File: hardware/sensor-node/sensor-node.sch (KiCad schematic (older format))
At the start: 51 parts, among them J1 CONUFL001-SMD-T, J2 Conn_ARM_JTAG_SWD_10, Q1 PMV250EPEA, U1 TLV61225, U2 TPS27081A, U3 SHT31-DIS, U4 24LC32, U5 MLX90614, U6 ADG633YCP, U7 TSV911RILT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

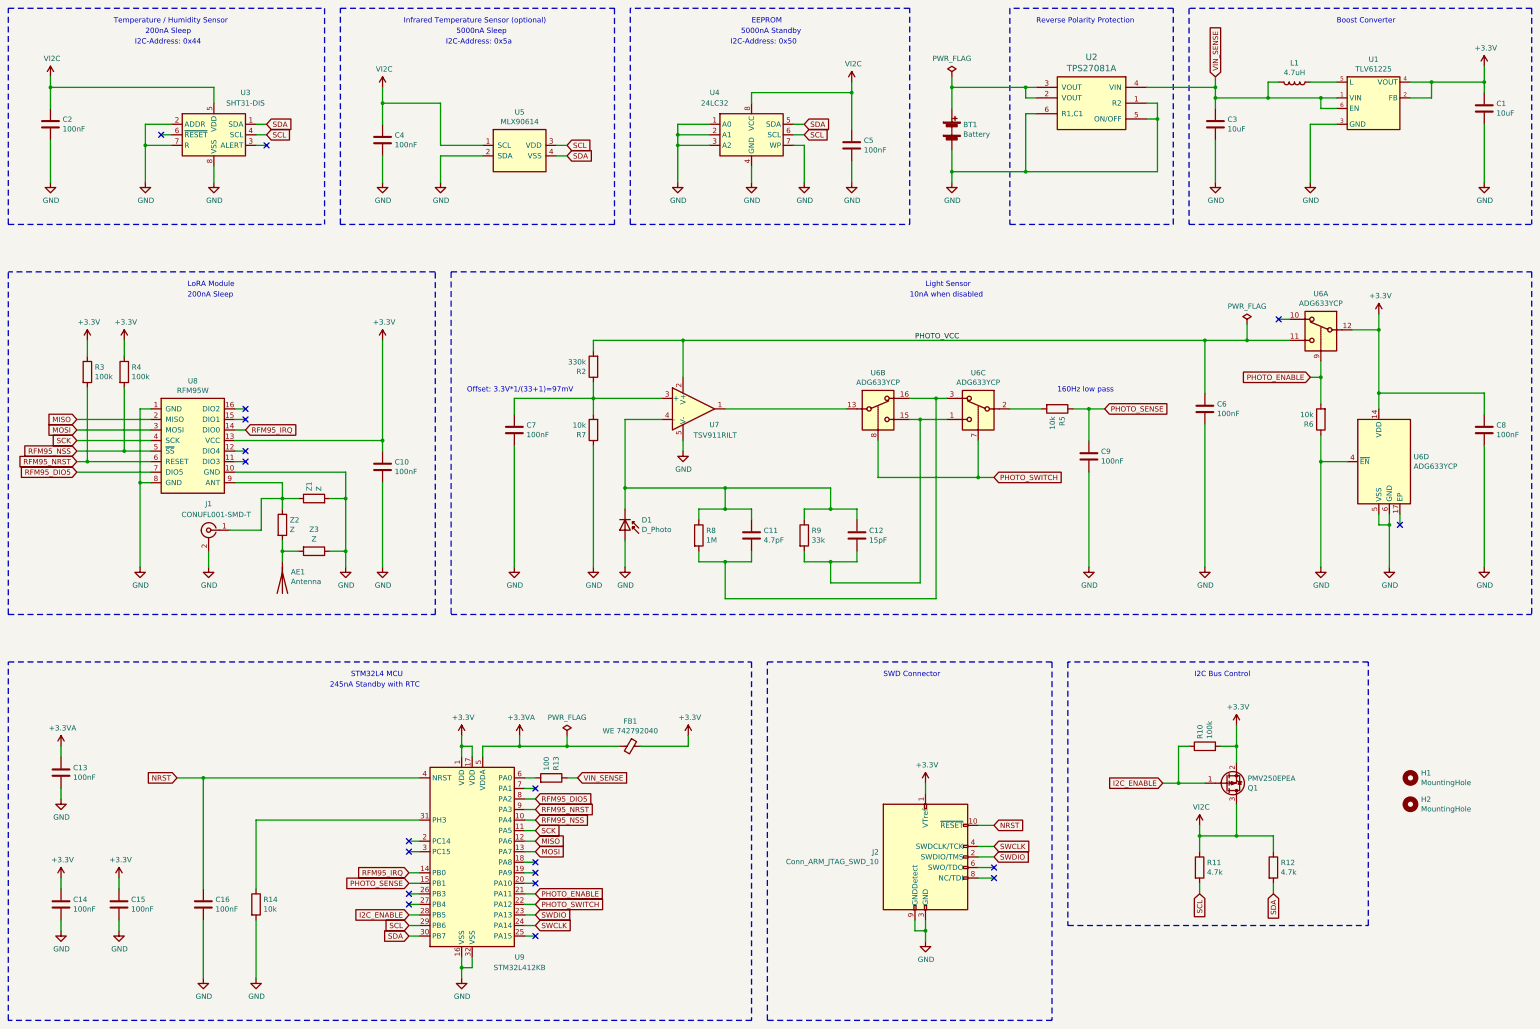
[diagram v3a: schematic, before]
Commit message: Fix ERC & DRC errors
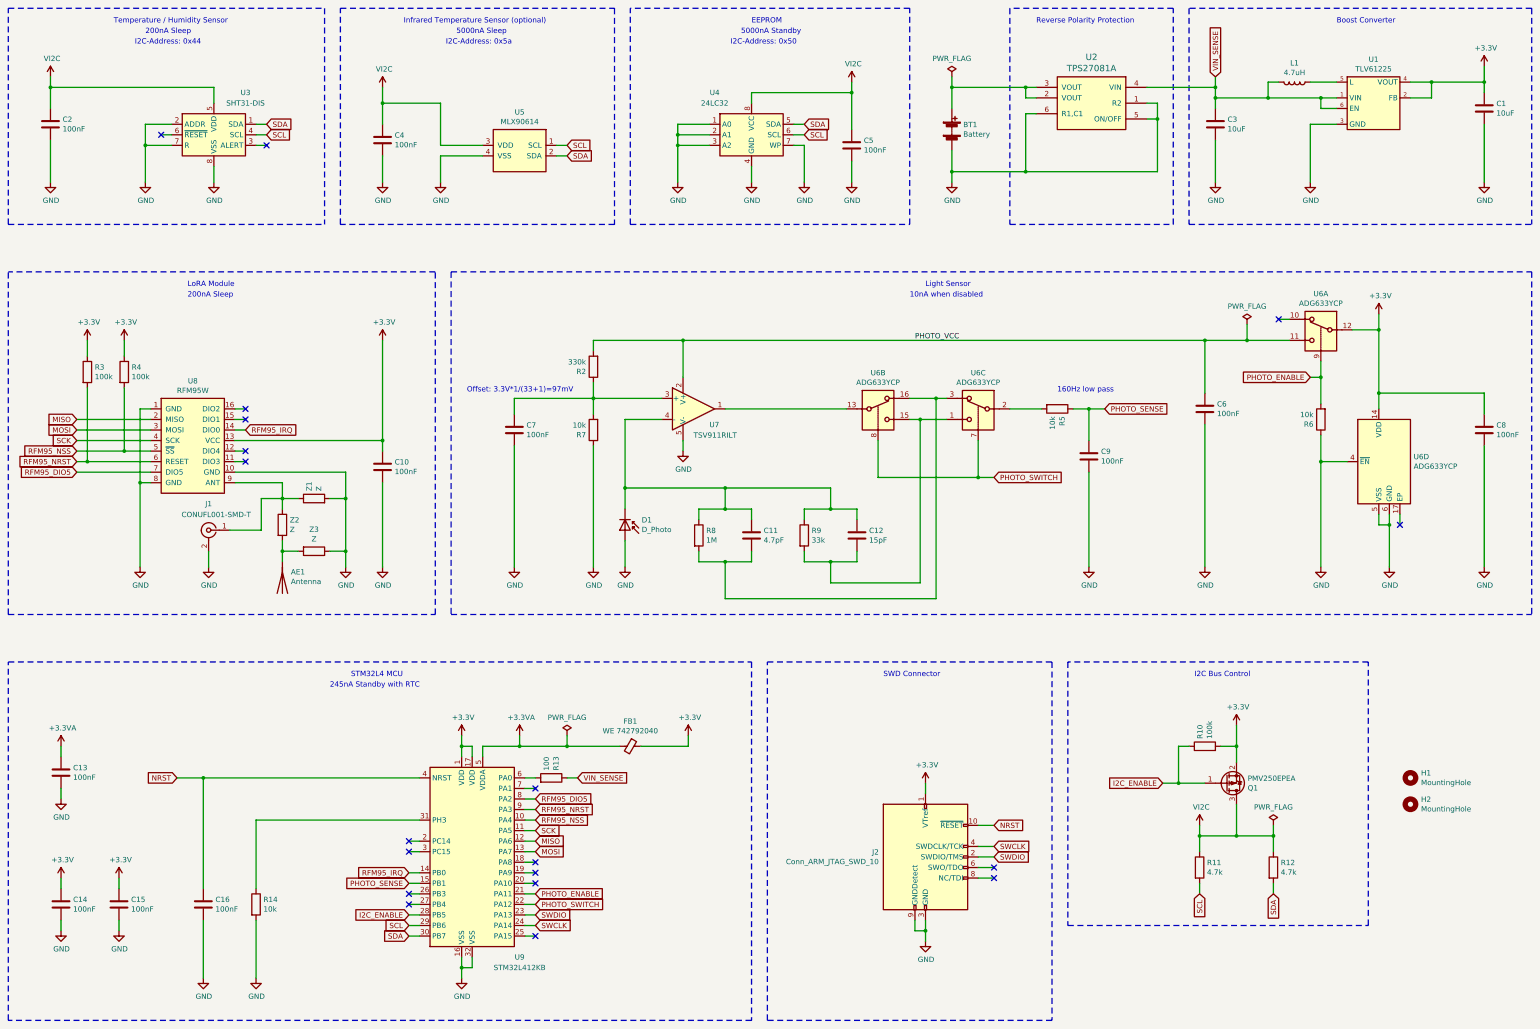
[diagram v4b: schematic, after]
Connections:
- net GND: now also U5.4 (VSS); no longer U5.2 (SDA)
- net SCL: now also U5.1 (SCL); no longer U5.3 (VDD)
- net SDA: now also U5.2 (SDA); no longer U5.4 (VSS)
- net VI2C: now also U5.3 (VDD); no longer U5.1 (SCL)
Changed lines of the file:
@@
 F 3 "" H 5900 2400 50  0001 C CNN
 	1    5900 2400
-	1    0    0    -1
+	-1   0    0    -1
 $EndComp
 Wire Wire Line
@@
 Wire Wire Line
 	14550 1750 15050 1750
+$Comp
+L power:PWR_FLAG #FLG0101
+U 1 1 5FCDF85F
+P 13050 8800
+F 0 "#FLG0101" H 13050 8875 50  0001 C CNN
+F 1 "PWR_FLAG" H 13050 8973 50  0000 C CNN
+F 2 "" H 13050 8800 50  0001 C CNN
+F 3 "~" H 13050 8800 50  0001 C CNN
+	1    13050 8800
+	1    0    0    -1
+$EndComp
+Wire Wire Line
+	13050 8800 13050 8900
+Connection ~ 13050 8900
 $EndSCHEMATC

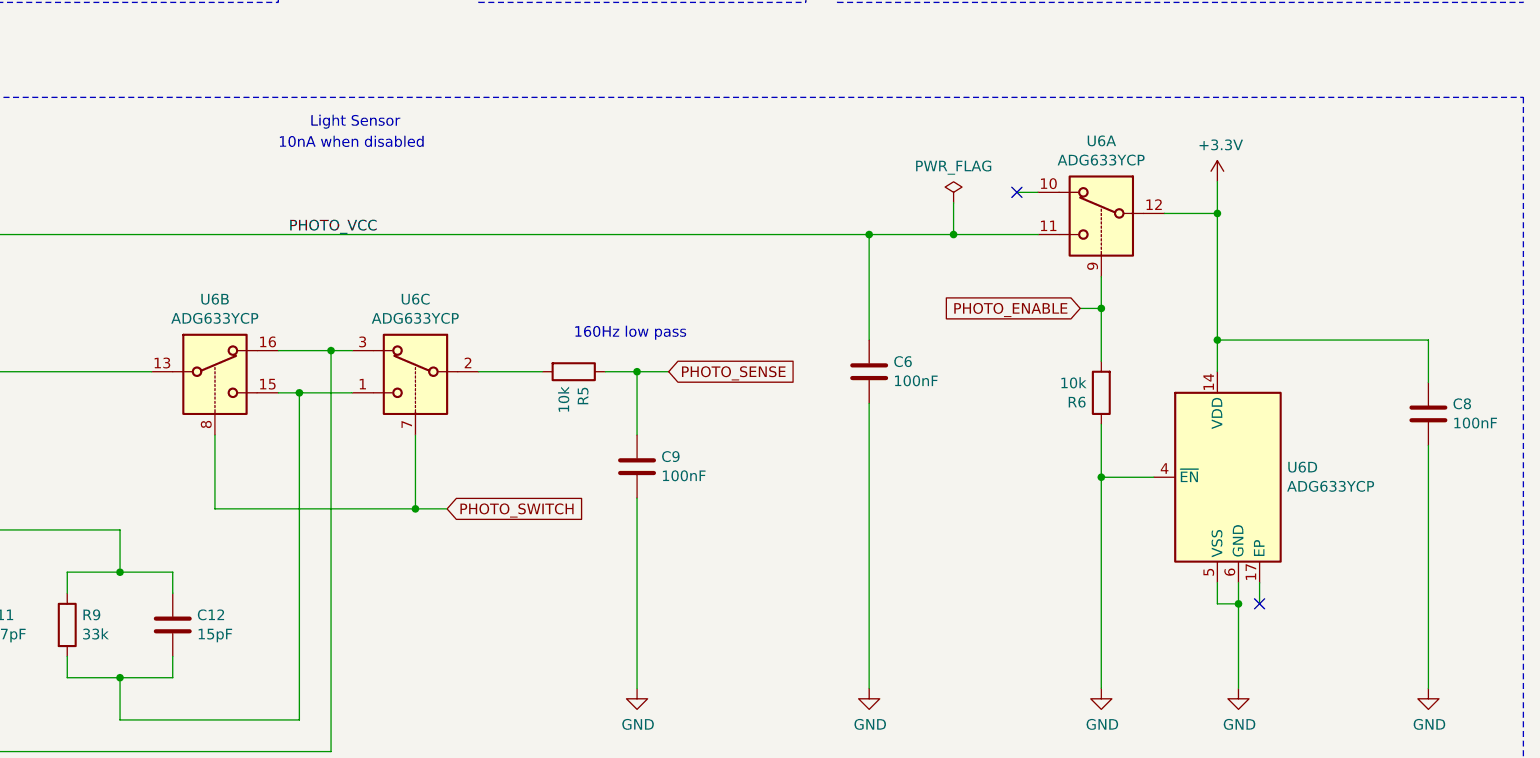
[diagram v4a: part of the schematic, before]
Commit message: Fix ADG633YRU pinout
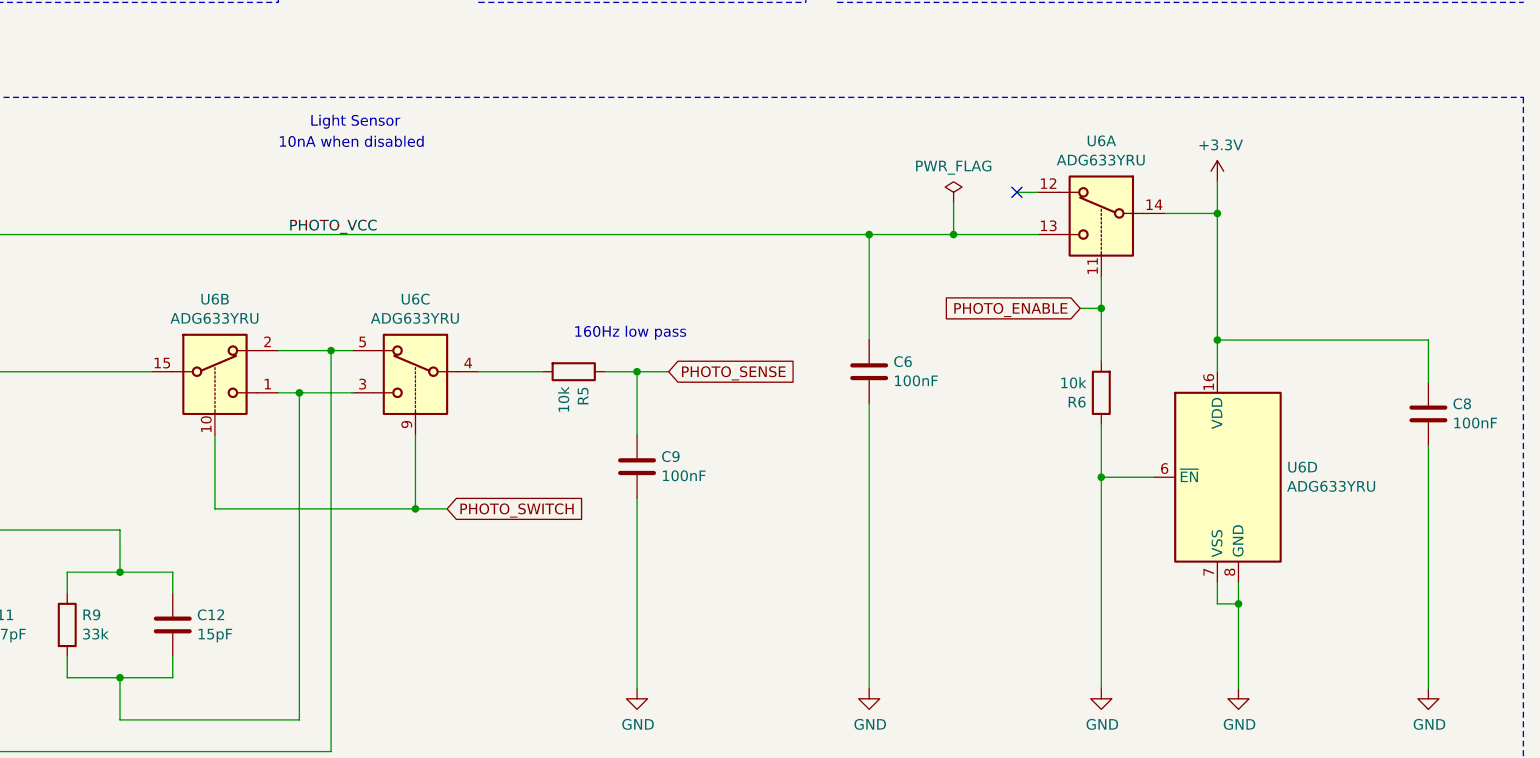
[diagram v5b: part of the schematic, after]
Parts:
- removed U6: ADG633YCP, Package_SO:TSSOP-16_4.4x5mm_P0.65mm, symbol Analog_Switch:ADG633YCP
- added U6: ADG633YRU, Package_SO:TSSOP-16_4.4x5mm_P0.65mm, symbol Analog_Switch:ADG633YRU
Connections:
- net +3V3: now also U6.14, U6.16 (VDD)
- net GND: now also U6.6 (~EN), U6.7 (VSS), U6.8 (GND)
- net PHOTO_ENABLE: now also U6.11
- net PHOTO_SWITCH: now also U6.10, U6.9
- net PHOTO_VCC: now also U6.13
- net at U7.1: now also U6.15
- net at C11.2, R8.2: now also U6.2, U6.5
- net at R5.2: now also U6.4
- net at C12.2, R9.2: now also U6.1, U6.3
- no-connect marks 19 -> 18
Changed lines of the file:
@@
 Wire Notes Line
 	6950 3100 9600 3100
-$Comp
-L Analog_Switch:ADG633YCP U6
-U 3 1 5FD12151
-P 10250 4750
-F 0 "U6" H 10250 4992 50  0000 C CNN
-F 1 "ADG633YCP" H 10250 4901 50  0000 C CNN
-F 2 "Package_SO:TSSOP-16_4.4x5mm_P0.65mm" H 10250 4750 50  0001 C CNN
-F 3 "" H 10250 4750 50  0001 C CNN
-	3    10250 4750
-	-1   0    0    -1
-$EndComp
-$Comp
-L Analog_Switch:ADG633YCP U6
-U 1 1 5FD14D71
-P 13500 4000
-F 0 "U6" H 13500 4242 50  0000 C CNN
-F 1 "ADG633YCP" H 13500 4151 50  0000 C CNN
-F 2 "Package_SO:TSSOP-16_4.4x5mm_P0.65mm" H 13500 4000 50  0001 C CNN
-F 3 "" H 13500 4000 50  0001 C CNN
-	1    13500 4000
-	-1   0    0    -1
-$EndComp
 Wire Wire Line
 	9600 4750 9850 4750
-Wire Wire Line
-	9950 4950 9700 4950
 Wire Wire Line
 	9300 5150 9300 5500
@@
 Wire Wire Line
 	8600 6200 8600 6300
-$Comp
-L Analog_Switch:ADG633YCP U6
-U 2 1 5FD0FC3F
-P 9300 4750
-F 0 "U6" H 9300 4992 50  0000 C CNN
-F 1 "ADG633YCP" H 9300 4901 50  0000 C CNN
-F 2 "Package_SO:TSSOP-16_4.4x5mm_P0.65mm" H 9300 4750 50  0001 C CNN
-F 3 "" H 9300 4750 50  0001 C CNN
-	2    9300 4750
-	1    0    0    -1
-$EndComp
 Wire Wire Line
 	10550 4850 10850 4850
@@
 	9700 4950 9600 4950
 Connection ~ 9850 4750
-Wire Wire Line
-	9850 4750 9950 4750
 Connection ~ 7850 6300
 Wire Wire Line
@@
 Text Notes 9600 3800 0    50   ~ 0
 10nA when disabled
-NoConn ~ 14250 5950
-Wire Wire Line
-	14250 5850 14250 5950
 Wire Wire Line
 	14150 5950 14150 5850
@@
 F 3 "~" H 15050 5050 50  0001 C CNN
 	1    15050 5050
-	1    0    0    -1
-$EndComp
-$Comp
-L Analog_Switch:ADG633YCP U6
-U 4 1 5FD16603
-P 14050 5350
-F 0 "U6" H 14380 5396 50  0000 L CNN
-F 1 "ADG633YCP" H 14380 5305 50  0000 L CNN
-F 2 "Package_SO:TSSOP-16_4.4x5mm_P0.65mm" H 14050 5350 50  0001 C CNN
-F 3 "" H 14050 5350 50  0001 C CNN
-	4    14050 5350
 	1    0    0    -1
 $EndComp
@@
 	13050 8800 13050 8900
 Connection ~ 13050 8900
+$Comp
+L Analog_Switch:ADG633YRU U6
+U 2 1 5FC55E5A
+P 9300 4750
+F 0 "U6" H 9300 4992 50  0000 C CNN
+F 1 "ADG633YRU" H 9300 4901 50  0000 C CNN
+F 2 "Package_SO:TSSOP-16_4.4x5mm_P0.65mm" H 9300 4750 50  0001 C CNN
+F 3 "https://www.analog.com/media/en/technical-documentation/data-sheets/ADG633.pdf" H 9300 4750 50  0001 C CNN
+	2    9300 4750
+	1    0    0    -1
+$EndComp
+$Comp
+L Analog_Switch:ADG633YRU U6
+U 1 1 5FC51273
+P 13500 4000
+F 0 "U6" H 13500 4242 50  0000 C CNN
+F 1 "ADG633YRU" H 13500 4151 50  0000 C CNN
+F 2 "Package_SO:TSSOP-16_4.4x5mm_P0.65mm" H 13500 4000 50  0001 C CNN
+F 3 "https://www.analog.com/media/en/technical-documentation/data-sheets/ADG633.pdf" H 13500 4000 50  0001 C CNN
+	1    13500 4000
+	-1   0    0    -1
+$EndComp
+Wire Wire Line
+	9850 4750 9950 4750
+Wire Wire Line
+	9950 4950 9700 4950
+$Comp
+L Analog_Switch:ADG633YRU U6
+U 3 1 5FC5A7C5
+P 10250 4750
+F 0 "U6" H 10250 4992 50  0000 C CNN
+F 1 "ADG633YRU" H 10250 4901 50  0000 C CNN
+F 2 "Package_SO:TSSOP-16_4.4x5mm_P0.65mm" H 10250 4750 50  0001 C CNN
+F 3 "https://www.analog.com/media/en/technical-documentation/data-sheets/ADG633.pdf" H 10250 4750 50  0001 C CNN
+	3    10250 4750
+	-1   0    0    -1
+$EndComp
+$Comp
+L Analog_Switch:ADG633YRU U6
+U 4 1 5FC64747
+P 14050 5350
+F 0 "U6" H 14380 5396 50  0000 L CNN
+F 1 "ADG633YRU" H 14380 5305 50  0000 L CNN
+F 2 "Package_SO:TSSOP-16_4.4x5mm_P0.65mm" H 14050 5350 50  0001 C CNN
+F 3 "https://www.analog.com/media/en/technical-documentation/data-sheets/ADG633.pdf" H 14050 5350 50  0001 C CNN
+	4    14050 5350
+	1    0    0    -1
+$EndComp
 $EndSCHEMATC

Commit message: Perform parts pinout check
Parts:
- AE1: value Antenna -> ANT-868-CHP-T; #manf (none) -> ANT-868-CHP-T; digikey# (none) -> ANT-868-CHP-TCT-ND; mouser# (none) -> 712-ANT-868-CHP-T
- BT1: value Battery -> Keystone-2468; #manf (none) -> 2468; digikey# (none) -> 36-2468-ND; mouser# (none) -> 534-2468
- C1, C3: #manf (none) -> C0805C106K9PAC7210; digikey# (none) -> 399-C0805C106K9PAC7210CT-ND; mouser# (none) -> 80-C0805C106K9P7210
- C10, C13, C14, C15, C16, C2, C4, C5, C6, C7, C8, C9: #manf (none) -> C0805C103K8RACTU; digikey# (none) -> C0805C103K8RAC7800; mouser# (none) -> 80-C0805C103K8R
- C11: #manf (none) -> C0805C479C8HACTU; digikey# (none) -> C0805C479C8HAC7800-ND; mouser# (none) -> 80-C0805C479C8HACTU
- C12: #manf (none) -> C0805C150M8HACTU; digikey# (none) -> C0805C150M8HAC7800; mouser# (none) -> 80-C0805C150M8HACTU
- D1: value D_Photo -> BPV10; #manf (none) -> BPV10; digikey# (none) -> 751-1001-ND; mouser# (none) -> 782-BPV10
- FB1: value WE 742792040 -> WE742792040; #manf (none) -> 742792040; digikey# (none) -> 732-1620-1-ND; mouser# (none) -> 710-742792040
- J1: #manf (none) -> CONUFL001-SMD-T; digikey# (none) -> CONUFL001-SMD-TCT-ND; mouser# (none) -> 712-CONUFL001-SMD-T
- J2: value Conn_ARM_JTAG_SWD_10 -> SHF-105-01-L-D-TH; #manf (none) -> SHF-105-01-L-D-TH; digikey# (none) -> SAM11769-ND; mouser# (none) -> 200-SHF10501LDTH
- L1: #manf (none) -> SRN4018TA-4R7M; digikey# (none) -> SRN4018TA-4R7MTR-ND; mouser# (none) -> 652-SRN4018TA-4R7M
- Q1: #manf (none) -> PMV250EPEA; digikey# (none) -> 1727-2303-1-ND; mouser# (none) -> 771-PMV250EPEAR
- R10, R3, R4: #manf (none) -> RC0805FR-07100KL; digikey# (none) -> 311-100KCRCT-ND; mouser# (none) -> 603-RC0805FR-07100KL
- R11, R12: #manf (none) -> RC0805FR-074K7L; digikey# (none) -> 311-4.70KCRCT-ND; mouser# (none) -> 603-RC0805FR-074K7L
- R13: #manf (none) -> RC0805FR-07100RL; digikey# (none) -> 311-100CRCT-ND; mouser# (none) -> 603-RC0805FR-07100RL
- R14, R5, R6, R7: #manf (none) -> RC0805FR-0710KL; digikey# (none) -> 311-10.0KCRCT-ND; mouser# (none) -> 603-RC0805FR-0710KL
- R2: #manf (none) -> RC0805FR-07330KL; digikey# (none) -> 311-330KCRCT-ND; mouser# (none) -> 603-RC0805FR-07330KL
- R8: #manf (none) -> RC0805FR-071ML; digikey# (none) -> 311-1.00MCRCT-ND; mouser# (none) -> 603-RC0805FR-071ML
- R9: #manf (none) -> RC0805FR-0733KL; digikey# (none) -> 311-33.0KCRCT-ND; mouser# (none) -> 603-RC0805FR-0733KL
- U1: #manf (none) -> TLV61225DCKR; digikey# (none) -> 296-36756-1-ND; mouser# (none) -> 595-TLV61225DCKR
- U2: #manf (none) -> TPS27081ADDCR; digikey# (none) -> 296-34970-1-ND; mouser# (none) -> 595-TPS27081ADDCR
- U3: #manf (none) -> SHT31-DIS-F2.5kS; digikey# (none) -> 1649-1066-1-ND; mouser# (none) -> 403-SHT31-DIS-F
- U4: #manf (none) -> 24LC32AT-I/SN; digikey# (none) -> 24LC32AT-I/SNCT-ND; mouser# (none) -> 579-24LC32AT-I/SN
- U5: #manf (none) -> MLX90614ESF-BCC-000-TU; digikey# (none) -> MLX90614ESF-BCC-000-TU-ND; mouser# (none) -> 482-90614ESFBCC000TU
- U6: #manf (none) -> ADG633YRUZ; digikey# (none) -> ADG633YRUZ-ND; mouser# (none) -> 584-ADG633YRUZ
- U7: #manf (none) -> TSV911RILT; digikey# (none) -> 497-10538-1-ND; mouser# (none) -> 511-TSV911RILT
- U8: #manf (none) -> RFM95W-868; digikey# (none) -> RFM95W-868S2-ND; mouser# (none) -> 223-RFM95W-868S2
- U9: #manf (none) -> STM32L412KBT6; digikey# (none) -> 497-18229-ND; mouser# (none) -> 511-STM32L412KBT6
